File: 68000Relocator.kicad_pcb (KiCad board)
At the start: 2 copper layers, 97.4 x 97.4 mm, 3 parts, among them P99 OSHW_LOGO, U1 68000D, U2 68000D

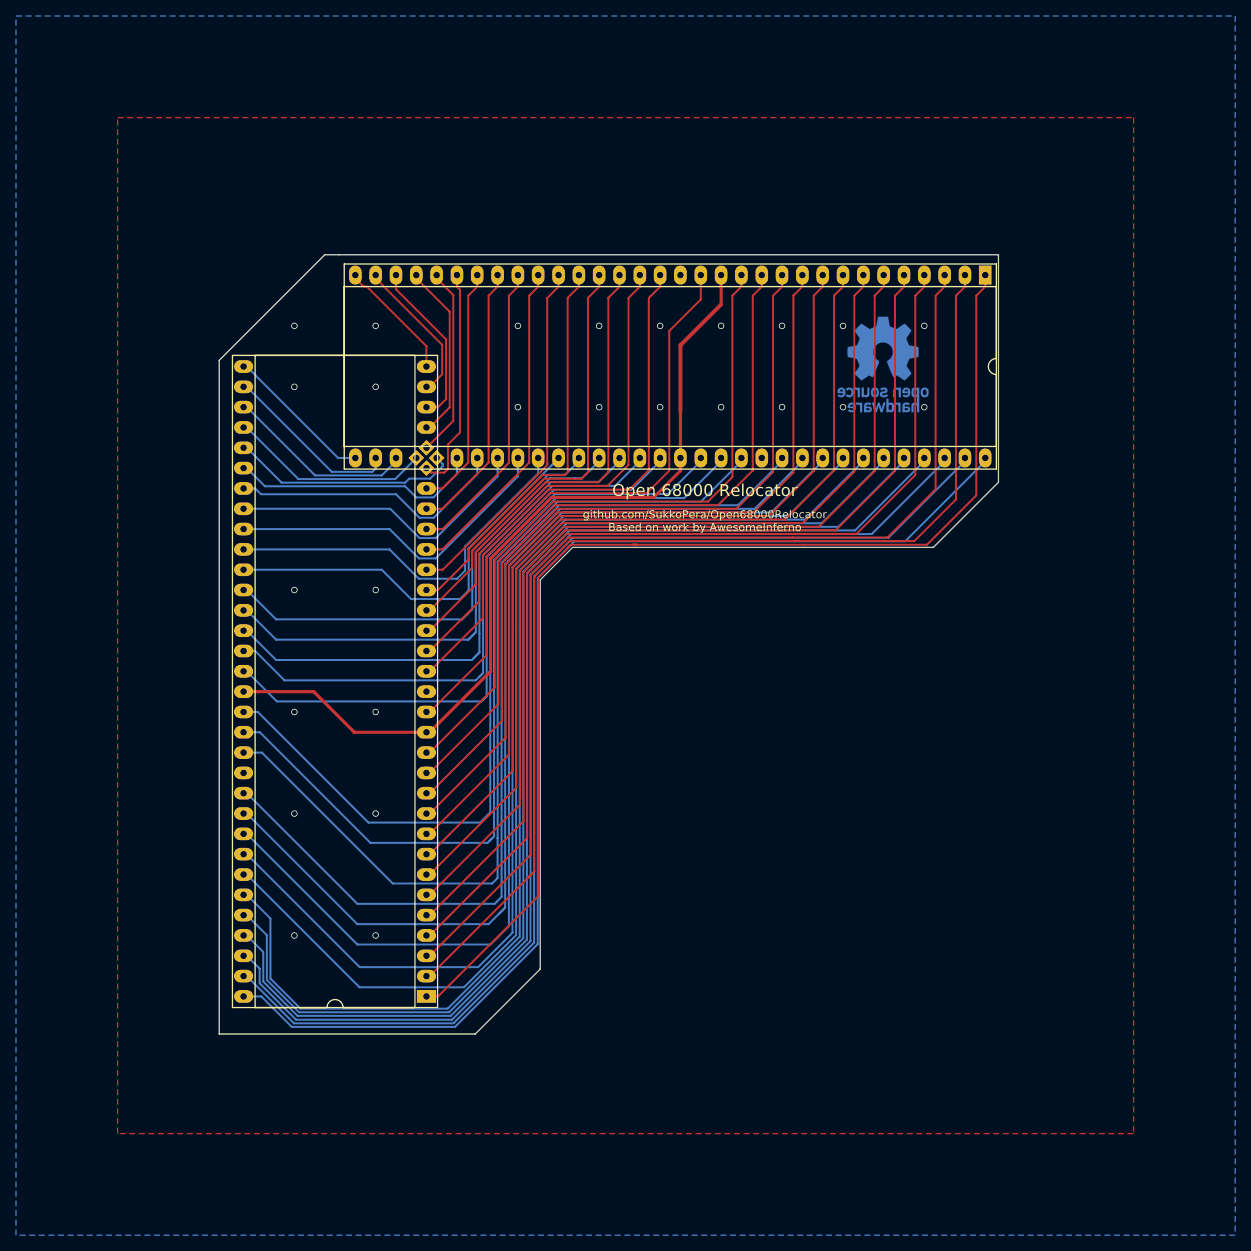
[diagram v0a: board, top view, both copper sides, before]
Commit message: Fix silkscreen and add version number
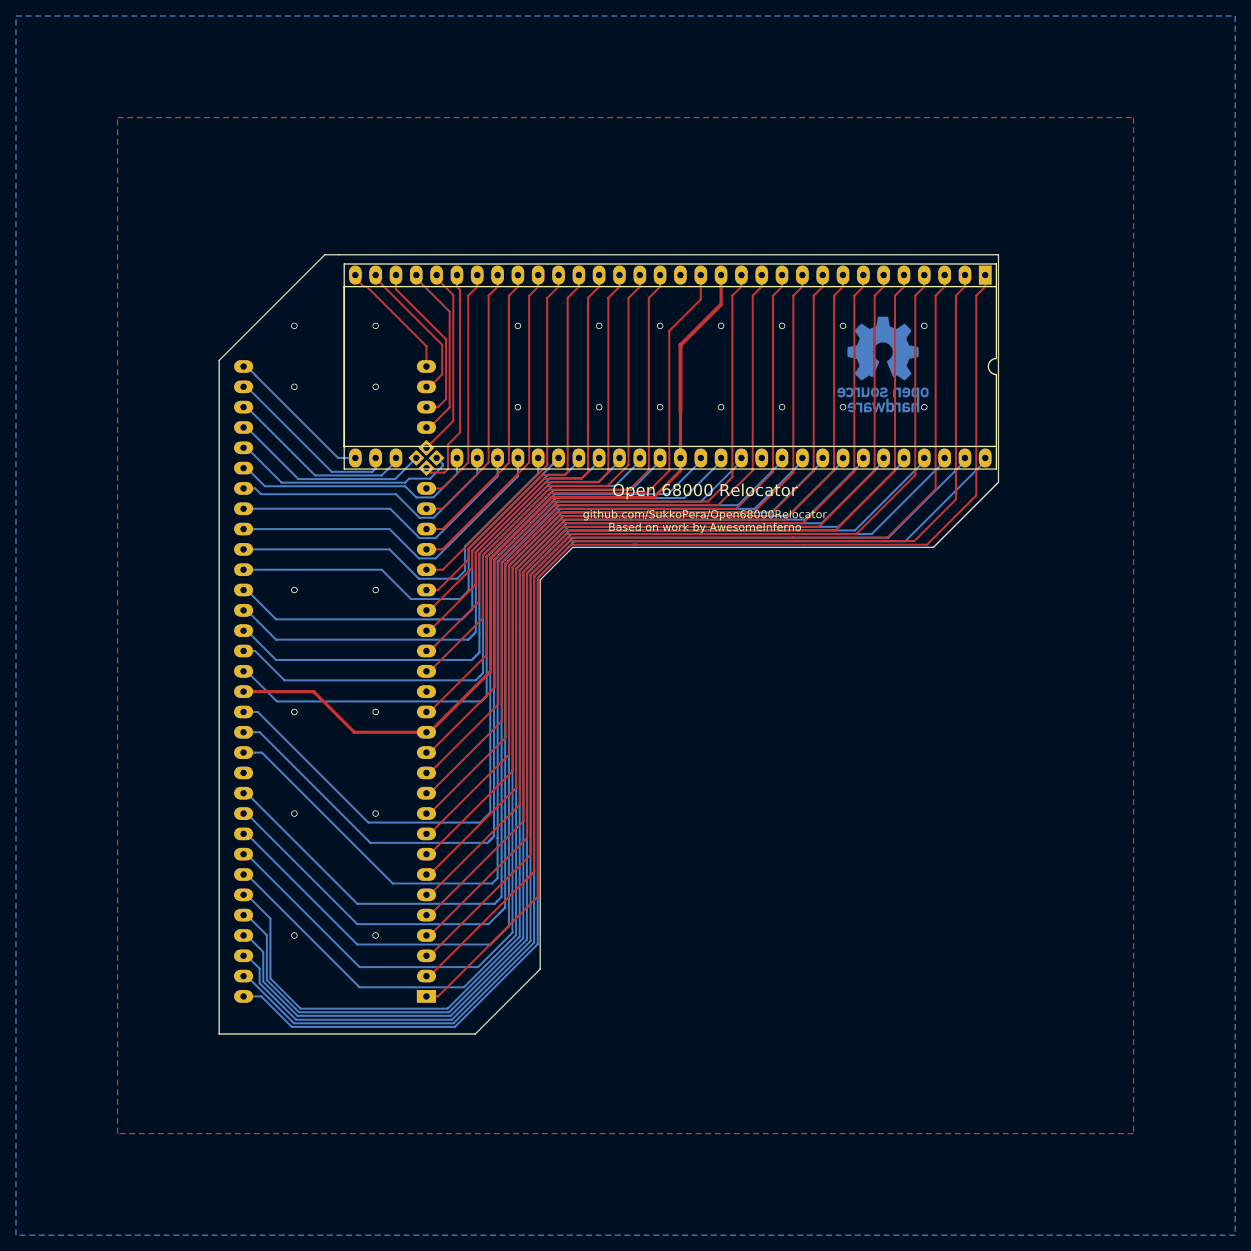
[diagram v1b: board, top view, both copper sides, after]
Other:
- board text added: "V1"

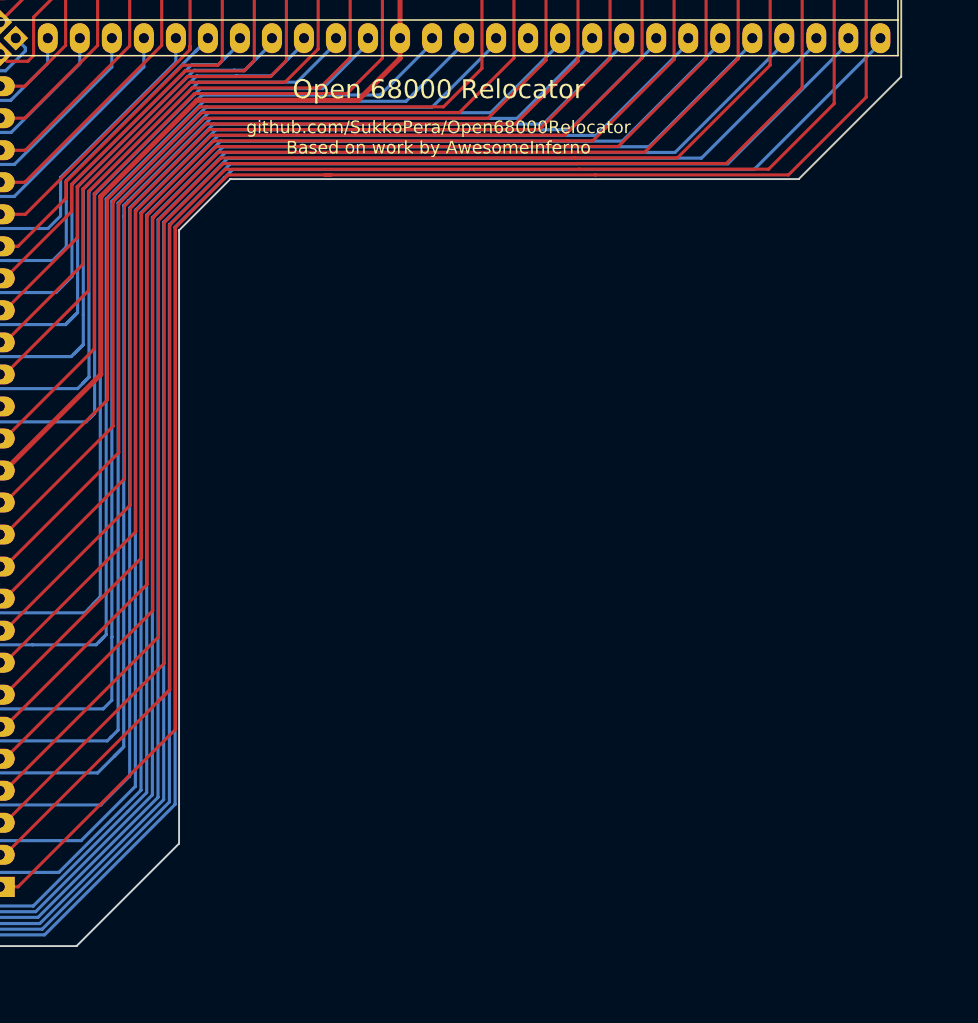
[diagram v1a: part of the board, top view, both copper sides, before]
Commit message: Make up some space between tracks and board edge
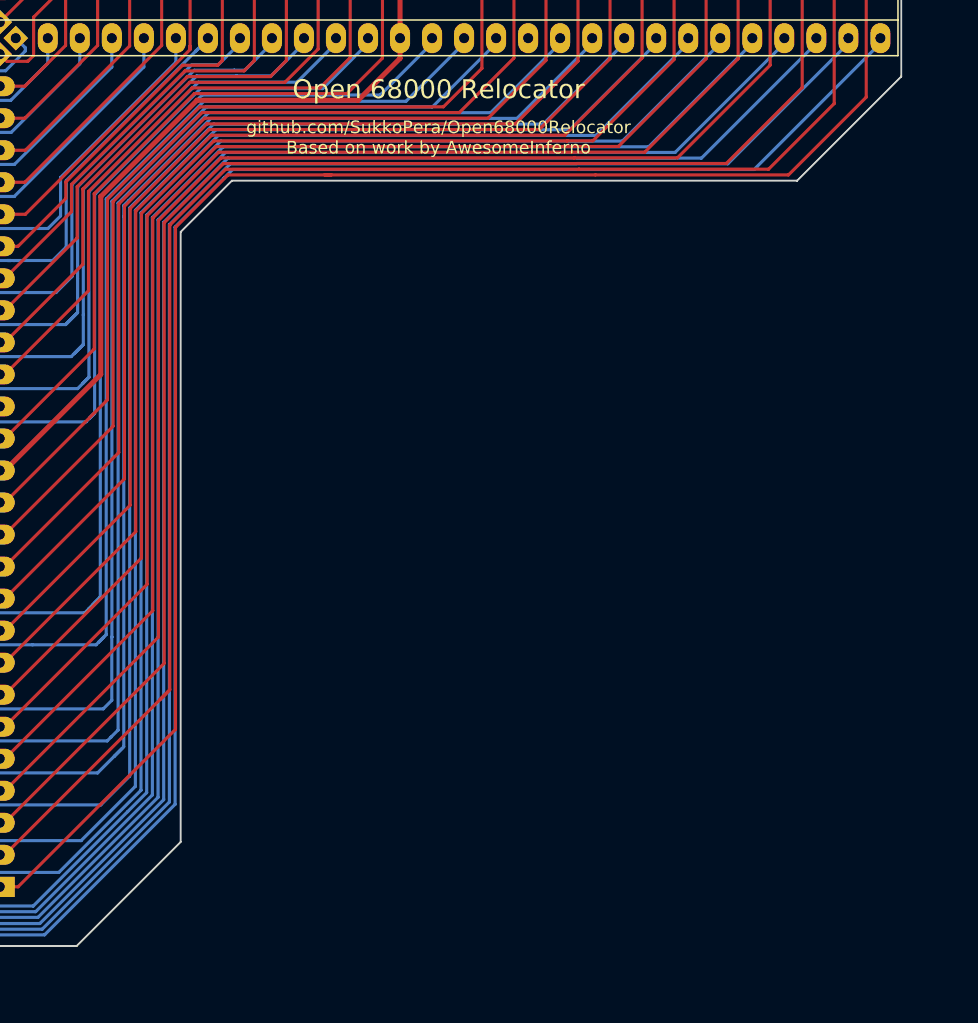
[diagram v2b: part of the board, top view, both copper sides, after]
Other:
- outline, holes or cut-outs redrawn
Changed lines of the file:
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@@
     (effects (font (size 1 1) (thickness 0.15)) (justify mirror))
   )
-  (gr_line (start 121.158 144.653) (end 129.286 136.525) (layer Edge.Cuts) (width 0.15))
+  (gr_line (start 121.158 144.653) (end 129.413 136.398) (layer Edge.Cuts) (width 0.15))
   (dimension 97.409 (width 0.3) (layer F.Fab)
     (gr_text "97,409 mm" (at 137.8585 39.429) (layer F.Fab)
@@
     (arrow2b (pts (xy 69.993938 47.244) (xy 70.580359 48.370504)))
   )
-  (gr_line (start 129.286 87.884) (end 133.35 83.82) (layer Edge.Cuts) (width 0.15))
-  (gr_line (start 178.435 83.82) (end 186.563 75.692) (layer Edge.Cuts) (width 0.15))
-  (gr_line (start 133.35 83.82) (end 178.435 83.82) (layer Edge.Cuts) (width 0.15))
-  (gr_line (start 129.286 136.525) (end 129.286 87.884) (layer Edge.Cuts) (width 0.15))
+  (gr_line (start 129.413 88.011) (end 133.477 83.947) (layer Edge.Cuts) (width 0.15))
+  (gr_line (start 178.308 83.947) (end 186.563 75.692) (layer Edge.Cuts) (width 0.15))
+  (gr_line (start 133.477 83.947) (end 178.308 83.947) (layer Edge.Cuts) (width 0.15))
+  (gr_line (start 129.413 136.398) (end 129.413 88.011) (layer Edge.Cuts) (width 0.15))
   (gr_line (start 102.362 47.244) (end 104.14 47.244) (layer Edge.Cuts) (width 0.15))
   (gr_line (start 89.154 60.452) (end 102.362 47.244) (layer Edge.Cuts) (width 0.15))
@@
       )
     )
+  )
+  (zone (net 0) (net_name "") (layer B.Cu) (hatch edge 0.508)
+    (connect_pads (clearance 0.1))
+    (min_thickness 0.254)
+    (keepout (tracks allowed) (vias allowed) (copperpour not_allowed))
+    (fill (arc_segments 16) (thermal_gap 0.508) (thermal_bridge_width 0.508))
+    (polygon
+      (pts
+        (xy 178.816 83.185) (xy 178.308 83.82) (xy 173.609 83.82) (xy 173.609 83.185)
+      )
+    )
